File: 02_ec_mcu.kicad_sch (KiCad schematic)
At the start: 48 parts, among them J16 Case power/reset button harne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, J4 TC2030 Cortex SWD: VTref/SWDI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, SW1 Reset, SW4 BOOT0 (DFU), U4 STM32F407VGTx, U44 TCA9539PWR resettable source 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, U46 SN74LVC1G08DBVR EC-reset-qual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, U5 TPS54202DDC, Y1 J32SMX-K-F-G-I-8M0 8MHz CL8pF, Y2 X1A000141000612 32.768kHz CL6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

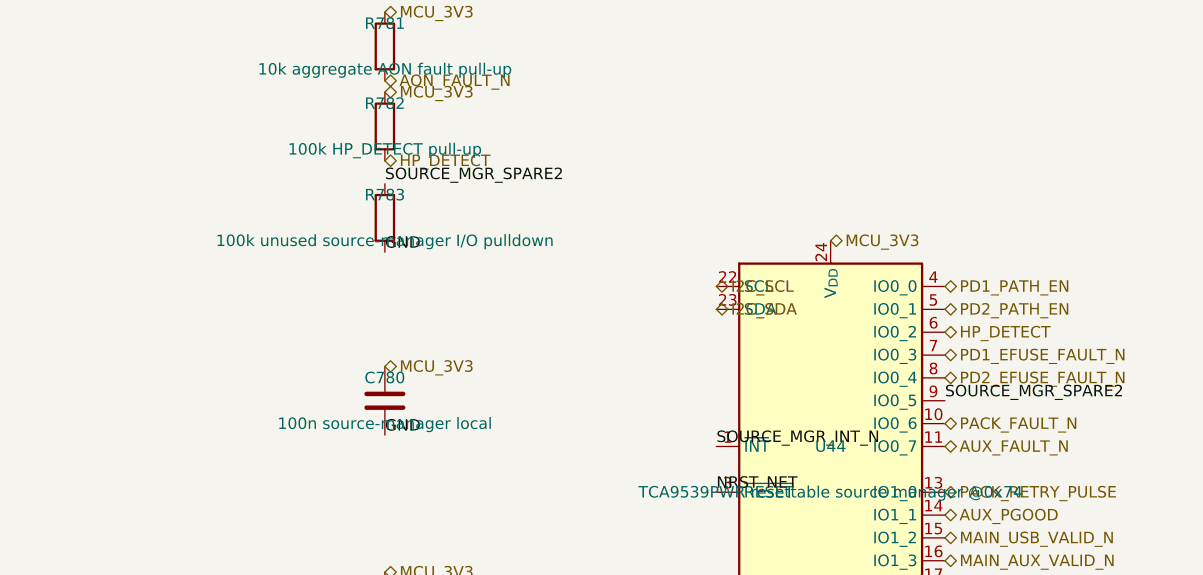
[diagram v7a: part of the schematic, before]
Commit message: Close remaining electronics-review items: FAN1_TAC, SLS_S3, SIO UART, F5/F6
- P2-2: fan FG (FAN_TACH, 8.2k MCU_3V3 pull-up) now feeds Mu FAN1_TAC
  (A1 pin 4; SIO GP52 tach input per LattePanda-Mu pin tables) so the
  module's thermal policy sees real fan speed
- P3-2: Mu SLS_S3 (A1 pin 7; SoC GPD5, high in S0/S3 per Mu pin tables)
  observed on the TCA9539 spare input; R783 100k default-low pulldown so an
  absent Mu reads off
- P3-1: Mu SIO console (3.3V Super I/O UART, SIO JP3/GP41) exposed on
  on-board probe pads TP16/TP17 with 100k MCU_3V3 idle pull-ups (R779/R784)
  on the rear service edge; EC has no spare UART-capable pin (documented)
- F5: move H15 (240,70) -> (252,70) per retention doc (was under the Mu
  courtyard); move SW4/R212 on-board at (185/196,180) (were off-board at
  y=195/200); npth_inside_courtyard cleared
- F6: apply DIFF_85/90/100 + USB2_45 net classes with the impedance-doc
  geometries and project-default 0.15mm clearance (idempotent apply);
  include DFU_CONN/EC_DFU USB2 pairs in USB2_45
- F7: verified already released (commits 91c4f3b/caf6ffb documented the
  ethernet notch + mounting pattern as contracts)
- Root-sheet builder: auto-expand sheet blocks to fit their pin count
- Pin-review contracts updated for the new A1/U44 wiring
- Verified: check_schematic self-check OK, ERC 0 errors, radio DB contracts
  OK, board DRC 0 electrical violations (shorts/mask-bridges/npth all 0),
  board-vs-schematic net parity 0 conflicts
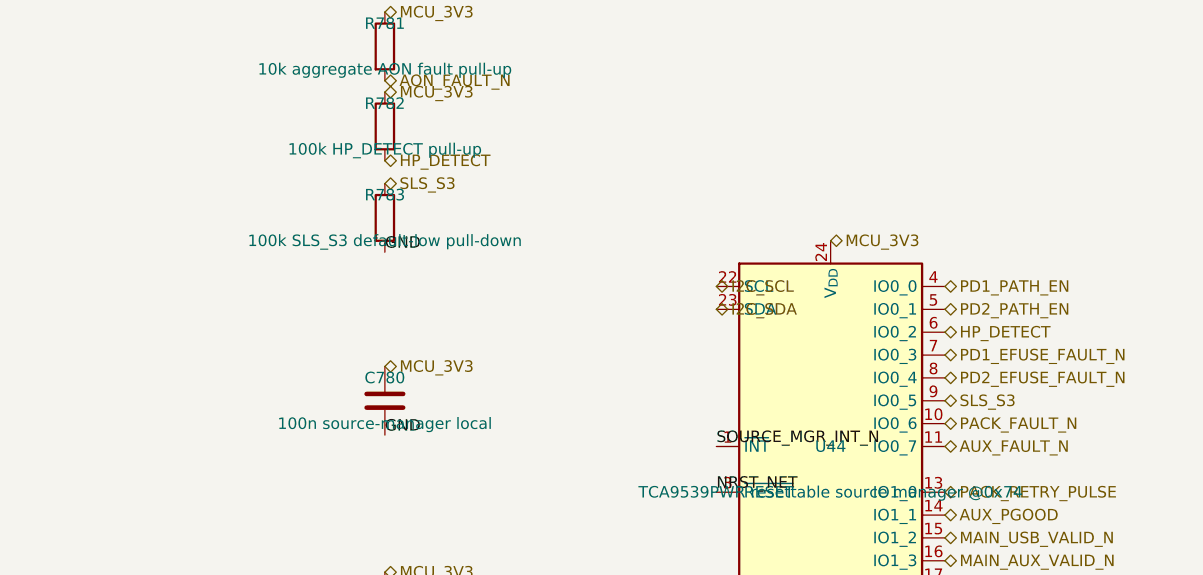
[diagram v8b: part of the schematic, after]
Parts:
- R783: value 100k unused source-manager I/O pulldown -> 100k SLS_S3 default-low pull-down
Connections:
- net SOURCE_MGR_SPARE2 renamed SLS_S3
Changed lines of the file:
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@@
   (effects (font (size 1.27 1.27)) (justify left bottom))
 )
-(label "SOURCE_MGR_SPARE2"
+(hierarchical_label "SLS_S3"
+  (shape bidirectional)
   (at 712.47 322.58 0)
   (effects (font (size 1.27 1.27)) (justify left bottom))
@@
   (dnp no)
   (property "Reference" "R783" (at 650.24 299.72 0) (effects (font (size 1.27 1.27))))
-  (property "Value" "100k unused source-manager I/O pulldown" (at 650.24 304.8 0) (effects (font (size 1.27 1.27))))
+  (property "Value" "100k SLS_S3 default-low pull-down" (at 650.24 304.8 0) (effects (font (size 1.27 1.27))))
   (property "Footprint" "Resistor_SMD:R_0603_1608Metric" (at 650.24 302.26 0) (effects (font (size 1.27 1.27)) (hide yes)))
   (property "Datasheet" "" (at 650.24 302.26 0) (effects (font (size 1.27 1.27)) (hide yes)))
@@
   )
 )
-(label "SOURCE_MGR_SPARE2"
+(hierarchical_label "SLS_S3"
+  (shape bidirectional)
   (at 650.24 298.45 0)
   (effects (font (size 1.27 1.27)) (justify left bottom))
